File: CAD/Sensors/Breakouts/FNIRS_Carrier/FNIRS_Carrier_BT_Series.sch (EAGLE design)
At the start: 36 parts, among them J1 62202021121, J2 62202021121, J3 20021111-00016T4LF, J4 20021111-00016T4LF, J5 20021111-00016T4LF, X1 TSW-108-07-G-S

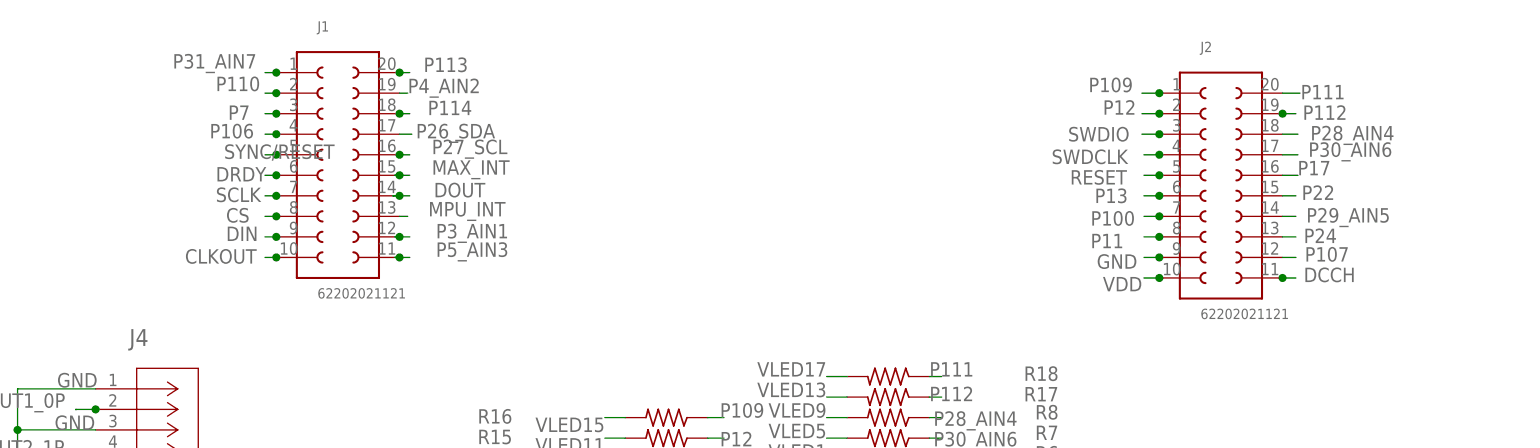
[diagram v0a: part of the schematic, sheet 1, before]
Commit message: modifed io order on bt840, some nrf52840 firmware cleanup (need to update with compass and audio too)
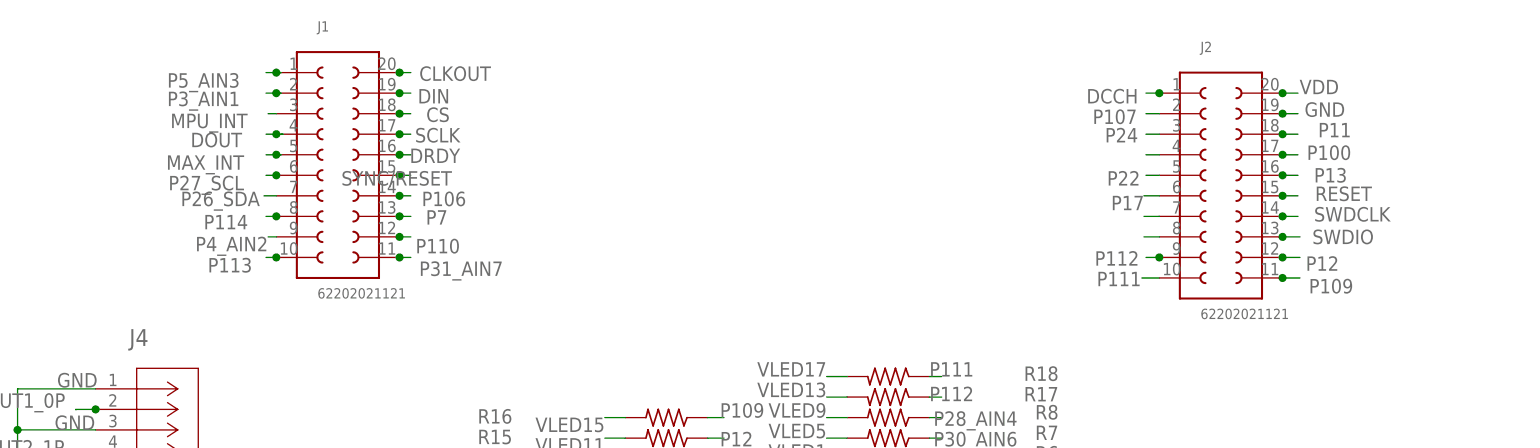
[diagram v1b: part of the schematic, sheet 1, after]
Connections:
- new net P28_AIN1: J2.8
- new net P29_AIN1: J2.4
- new net P30_AIN1: J2.7
- net CLKOUT: now also J1.20; no longer J1.10
- net CS: now also J1.18; no longer J1.8
- net DCCH: now also J2.1; no longer J2.11
- net DIN: now also J1.19; no longer J1.9
- net DOUT: now also J1.4; no longer J1.14
- net DRDY: now also J1.16; no longer J1.6
- net GND: now also J2.19; no longer J2.9
- net MAX_INT: now also J1.5; no longer J1.15
- net MPU_INT: now also J1.3; no longer J1.13
- net P100: now also J2.17; no longer J2.7
- net P106: now also J1.14; no longer J1.4
- net P107: now also J2.2; no longer J2.12
- net P109: now also J2.11; no longer J2.1
- net P11: now also J2.18; no longer J2.8
- net P110: now also J1.12; no longer J1.2
- net P111: now also J2.10; no longer J2.20
- net P112: now also J2.9; no longer J2.19
- net P113: now also J1.10; no longer J1.20
- net P114: now also J1.8; no longer J1.18
- net P12: now also J2.12; no longer J2.2
- net P13: now also J2.16; no longer J2.6
- net P17: now also J2.6; no longer J2.16
- net P22: now also J2.5; no longer J2.15
- net P24: now also J2.3; no longer J2.13
- net P26_SDA: now also J1.7; no longer J1.17
- net P27_SCL: now also J1.6; no longer J1.16
- net P28_AIN4: no longer J2.18
- net P29_AIN5: no longer J2.14
- net P30_AIN6: no longer J2.17
- net P31_AIN7: now also J1.11; no longer J1.1
- net P3_AIN1: now also J1.2; no longer J1.12
- net P4_AIN2: now also J1.9; no longer J1.19
- net P5_AIN3: now also J1.1; no longer J1.11
- net P7: now also J1.13; no longer J1.3
- net RESET: now also J2.15; no longer J2.5
- net SCLK: now also J1.17; no longer J1.7
- net SWDCLK: now also J2.14; no longer J2.4
- net SWDIO: now also J2.13; no longer J2.3
- net SYNC/RESET: now also J1.15; no longer J1.5
- net VDD: now also J2.20; no longer J2.10

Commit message: fixed fnirs carrier board
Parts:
- removed J3, J4, J5: 20021111-00016T4LF, 2x8_1.27mm:20021111-00016T4LF
- added J6, J7, J8: FTSH-108-02-LM-D-ES, 16pos1.27mm:FTSH-108-02-LM-D-ES
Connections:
- removed net 0P: J3.2, J5.2
- removed net 1P: J3.4, J5.4
- removed net 2P: J3.6, J5.6
- removed net 3P: J3.8, J5.8
- removed net 4P: J3.10, J5.10
- removed net 5P: J3.12, J5.12
- removed net 6P: J3.14, J5.14
- removed net 7P: J3.16, J5.16
- removed net P28_AIN1: J2.8
- removed net P28_AIN4: R8.1
- removed net P29_AIN1: J2.4
- removed net P29_AIN5: R4.1
- removed net P30_AIN1: J2.7
- removed net P30_AIN6: R7.1
- new net P28_AIN: J2.8, R11.1
- new net P29_AIN: J2.4, R9.1
- new net P30_AIN: J2.7, R4.1
- net AOUT1_0P: now also J6.01, J7.01, J8.15; no longer J4.2
- net AOUT2_1P: now also J6.03, J7.03, J8.13; no longer J4.4
- net AOUT3_2P: now also J6.05, J7.05, J8.11; no longer J4.6
- net AOUT4_3P: now also J6.07, J7.07, J8.09; no longer J4.8
- net AOUT5_4P: now also J6.09, J7.09, J8.07; no longer J4.10
- net AOUT6_5P: now also J6.11, J7.11, J8.05; no longer J4.12
- net AOUT7_6P: now also J6.13, J7.13, J8.03; no longer J4.14
- net AOUT8_7P: now also J6.15, J7.15, J8.01; no longer J4.16
- net GND: now also J6.02, J6.04, J6.06, J6.08, J6.10, J6.12, J6.14, J6.16, J7.02, J7.04, J7.06, J7.08, J7.10, J7.12, J7.14, J7.16, J8.02, J8.04, J8.06, J8.08, J8.10, J8.12, J8.14, J8.16; no longer J3.1, J3.11, J3.13, J3.15, J3.3, J3.5, J3.7, J3.9, J4.1, J4.11, J4.13, J4.15, J4.3, J4.5, J4.7, J4.9, J5.1, J5.11, J5.13, J5.15, J5.3, J5.5, J5.7, J5.9
- net P100: no longer R13.1
- net P106: now also R8.1
- net P107: now also R1.1; no longer R2.1
- net P109: now also R12.1; no longer R16.1
- net P11: no longer R1.1
- net P110: now also R7.1
- net P111: now also R5.1; no longer R18.1
- net P112: no longer R17.1
- net P113: now also R18.1; no longer R11.1
- net P114: no longer R9.1
- net P12: now also R6.1; no longer R15.1
- net P13: no longer R14.1
- net P17: now also R10.1; no longer R6.1
- net P22: now also R3.1; no longer R5.1
- net P24: now also R2.1; no longer R3.1
- net P31_AIN7: now also R13.1; no longer R12.1
- net P3_AIN1: now also R17.1
- net P4_AIN2: now also R16.1; no longer R10.1
- net P5_AIN3: now also R15.1
- net P7: now also R14.1
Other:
- note added: "ADC 0 jumper"
- note added: "Connector to 16 ch"
- note added: "Pinouts are specified for BT840 but are compatible with BT40 if you follow renaming conventions in the Datasheet"
- note added: "TODO: replace GPIO with the LED driver"
- moved on the sheet: J1, J2, R1, R10, R11, R12, R13, R14, R15, R16, R17, R18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
